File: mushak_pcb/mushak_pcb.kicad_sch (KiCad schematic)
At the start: 45 parts, among them J1 Conn_01x04_Male, J10 IR_1, J11 AS5600_1, J12 IR_2, J13 AS5600_2, J14 IR_3, J15 ToF, J16 IR_4, J2 Conn_01x02_Female, J3 BLE_Conn, Q1 DMN3065LW-7, SW1 SW_Push, SW2 SW_Push, U2 TLV1117LV30DCYT, U6 STM32F405RGTx, Y1 25Mhz, Y2 32.769kHz

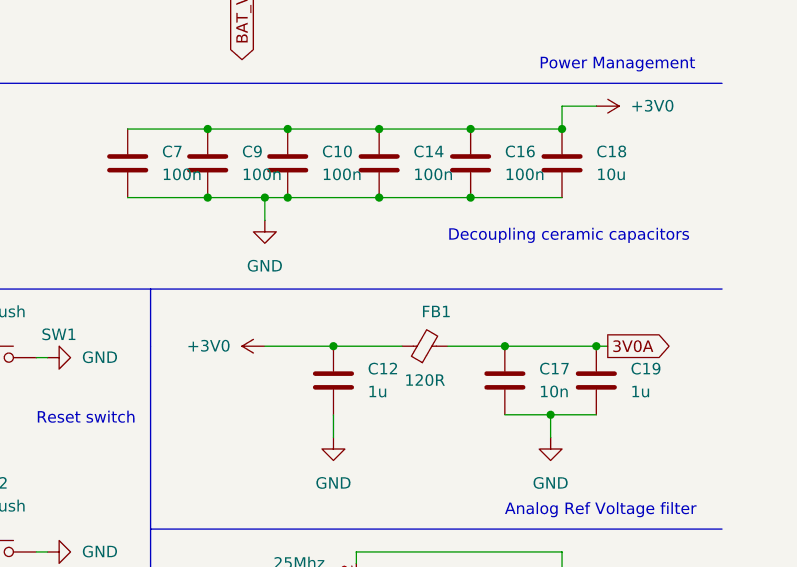
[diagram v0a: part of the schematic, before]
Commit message: changed footprints of capacitors and resistors
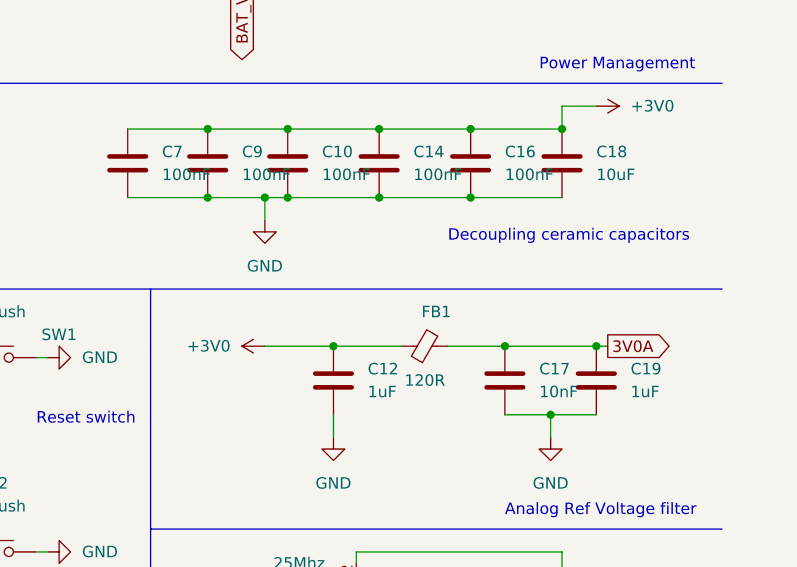
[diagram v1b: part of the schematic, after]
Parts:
- C10, C16, C7, C9: value 100n -> 100nF; footprint Capacitor_SMD:C_0402_1005Metric -> Capacitor_SMD:C_0201_0603Metric
- C12, C19: value 1u -> 1uF
- C13, C8: footprint Capacitor_SMD:C_0402_1005Metric -> Capacitor_SMD:C_0805_2012Metric
- C14: value 100n -> 100nF
- C17: value 10n -> 10nF
- C18: value 10u -> 10uF
- C3, C4: footprint Capacitor_SMD:C_0402_1005Metric -> Capacitor_SMD:C_0201_0603Metric
- R1, R4: footprint Resistor_SMD:R_0402_1005Metric -> Resistor_SMD:R_0603_1608Metric
- R2, R3: footprint Resistor_SMD:R_0402_1005Metric -> Resistor_SMD:R_0201_0603Metric

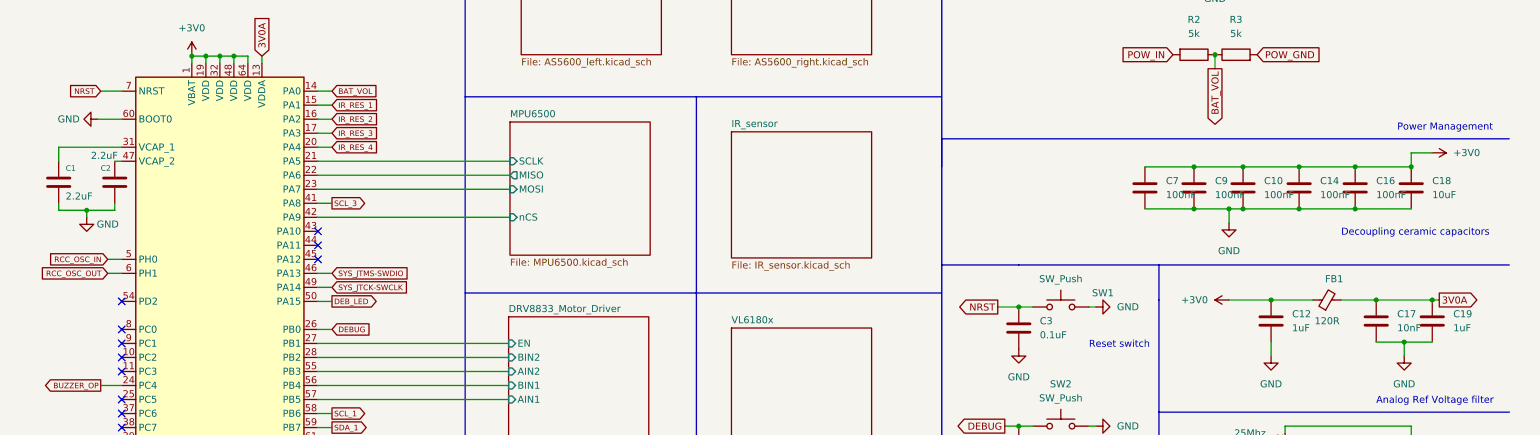
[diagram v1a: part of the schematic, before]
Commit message: made draft pcb footprint placement
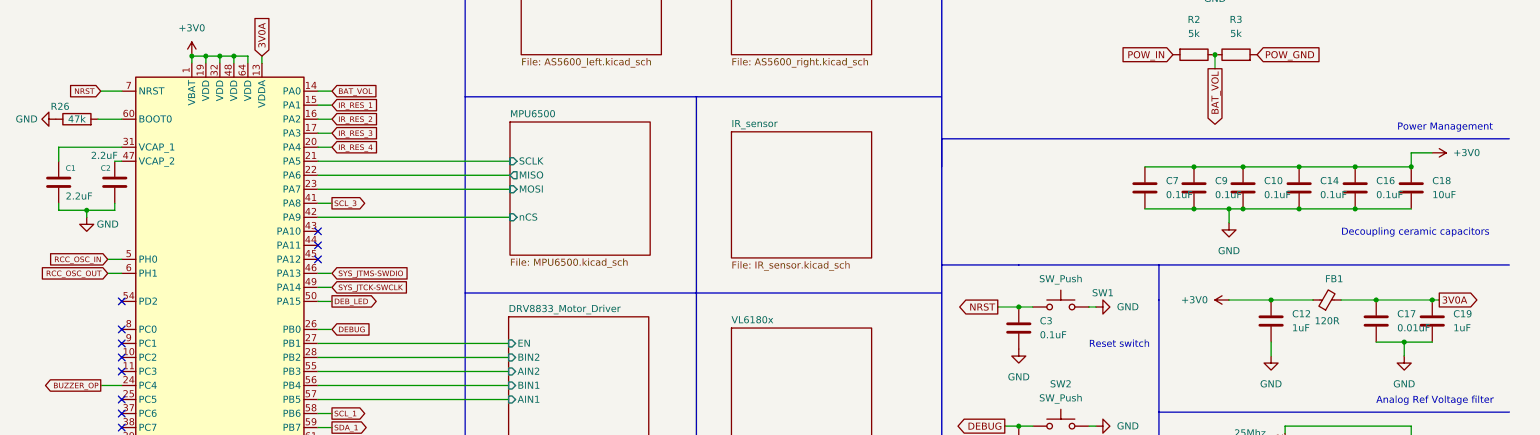
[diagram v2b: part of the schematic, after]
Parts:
- added R26: 47k, Resistor_SMD:R_0201_0603Metric, symbol Device:R
- C10, C14, C16, C7, C9: value 100nF -> 0.1uF
- C17: value 10nF -> 0.01uF
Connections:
- net GND: now also R26.1; no longer U6.60 (BOOT0)
- new net: R26.2, U6.60 (BOOT0)

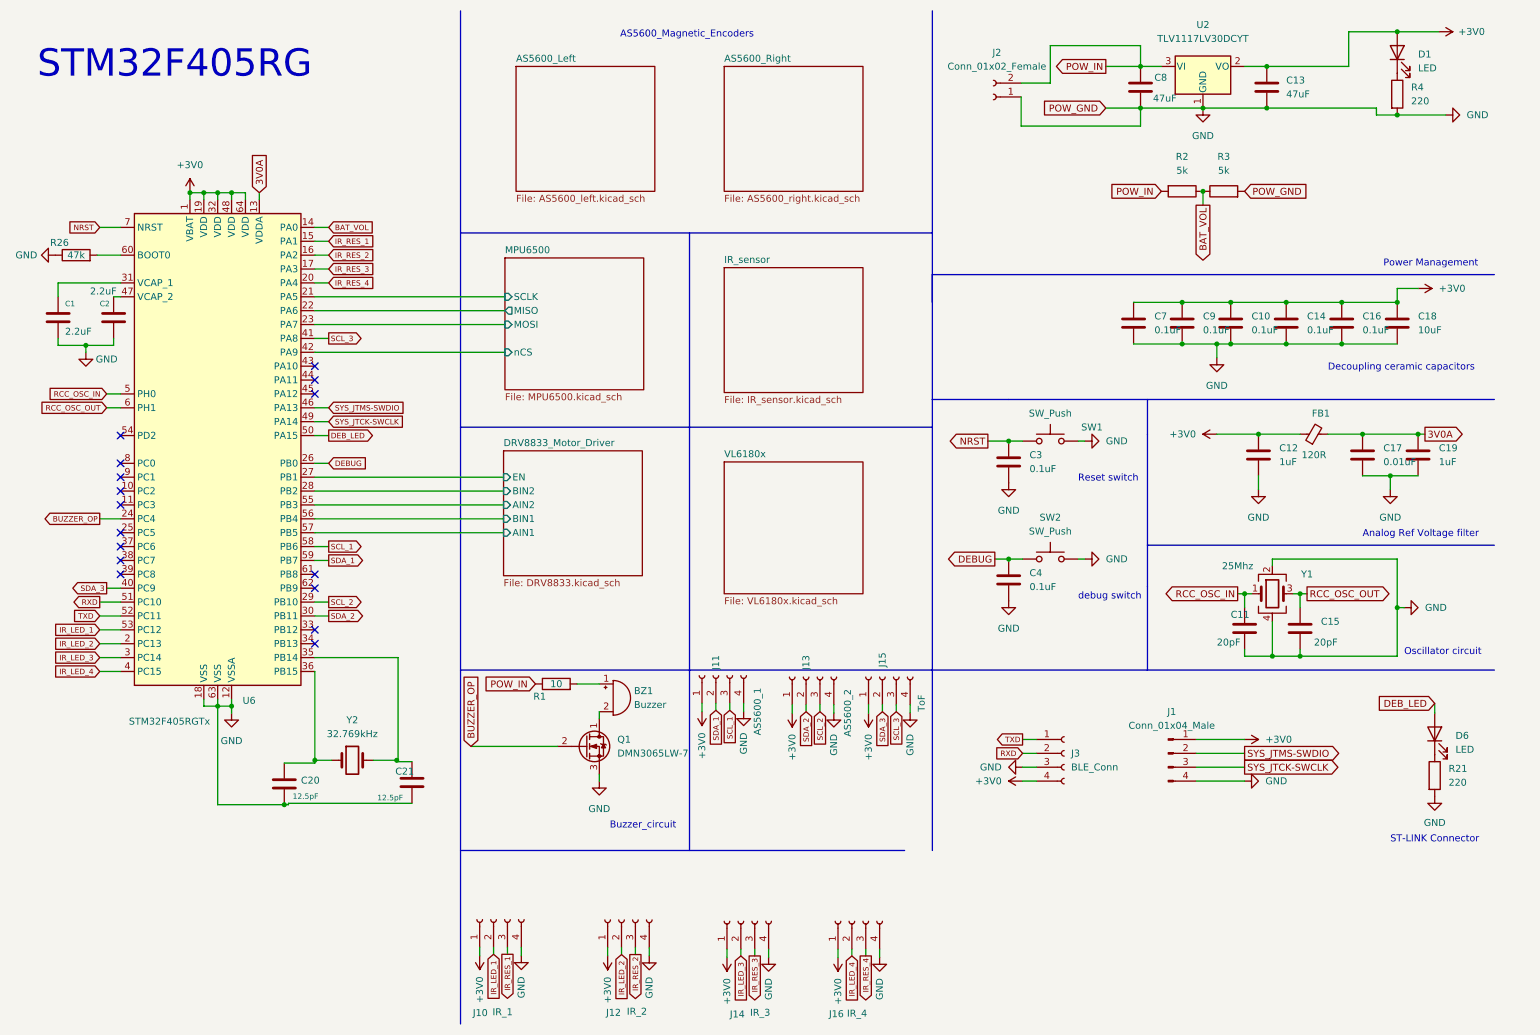
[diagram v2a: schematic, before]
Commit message: Add 3d models to footprint
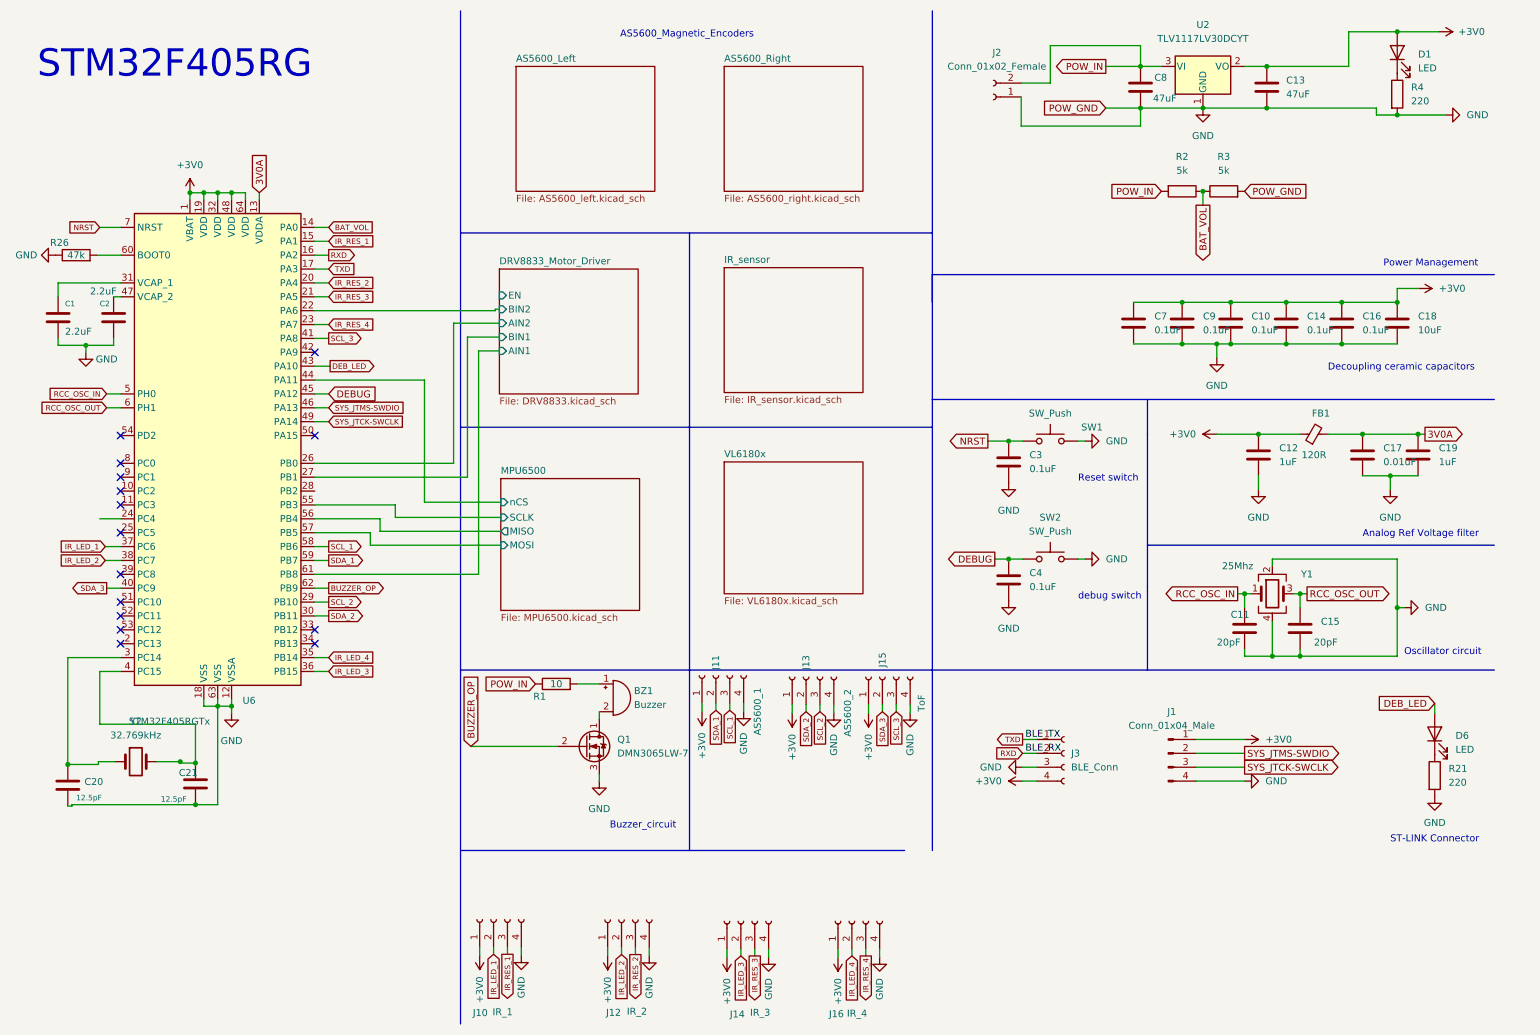
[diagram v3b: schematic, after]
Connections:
- net BUZZER_OP: now also U6.62 (PB9); no longer U6.24 (PC4)
- net DEBUG: now also U6.45 (PA12); no longer U6.26 (PB0)
- net DEB_LED: now also U6.43 (PA10); no longer U6.50 (PA15)
- net DRV8833_Motor_Driver/AIN1: now also U6.61 (PB8); no longer U6.57 (PB5)
- net DRV8833_Motor_Driver/AIN2: now also U6.26 (PB0); no longer U6.55 (PB3)
- net DRV8833_Motor_Driver/BIN1: now also U6.27 (PB1); no longer U6.56 (PB4)
- net DRV8833_Motor_Driver/BIN2: now also U6.22 (PA6); no longer U6.28 (PB2)
- net DRV8833_Motor_Driver/EN: no longer U6.27 (PB1)
- net IR_LED_1: now also U6.37 (PC6); no longer U6.53 (PC12)
- net IR_LED_2: now also U6.38 (PC7); no longer U6.2 (PC13)
- net IR_LED_3: now also U6.36 (PB15); no longer U6.3 (PC14)
- net IR_LED_4: now also U6.35 (PB14); no longer U6.4 (PC15)
- net IR_RES_2: now also U6.20 (PA4); no longer U6.16 (PA2)
- net IR_RES_3: now also U6.21 (PA5); no longer U6.17 (PA3)
- net IR_RES_4: now also U6.23 (PA7); no longer U6.20 (PA4)
- net MPU6500/MISO: now also U6.56 (PB4); no longer U6.22 (PA6)
- net MPU6500/MOSI: now also U6.57 (PB5); no longer U6.23 (PA7)
- net MPU6500/SCLK: now also U6.55 (PB3); no longer U6.21 (PA5)
- net MPU6500/nCS: now also U6.44 (PA11); no longer U6.42 (PA9)
- net RXD: now also U6.16 (PA2); no longer U6.51 (PC10)
- net TXD: now also U6.17 (PA3); no longer U6.52 (PC11)
- net at C20.1, Y2.1: now also U6.3 (PC14); no longer U6.36 (PB15)
- net at C21.1, Y2.2: now also U6.4 (PC15); no longer U6.35 (PB14)
- no-connect marks 16 -> 15
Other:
- moved on the sheet: C20, C21, Y2

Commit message: updated footprint for motors
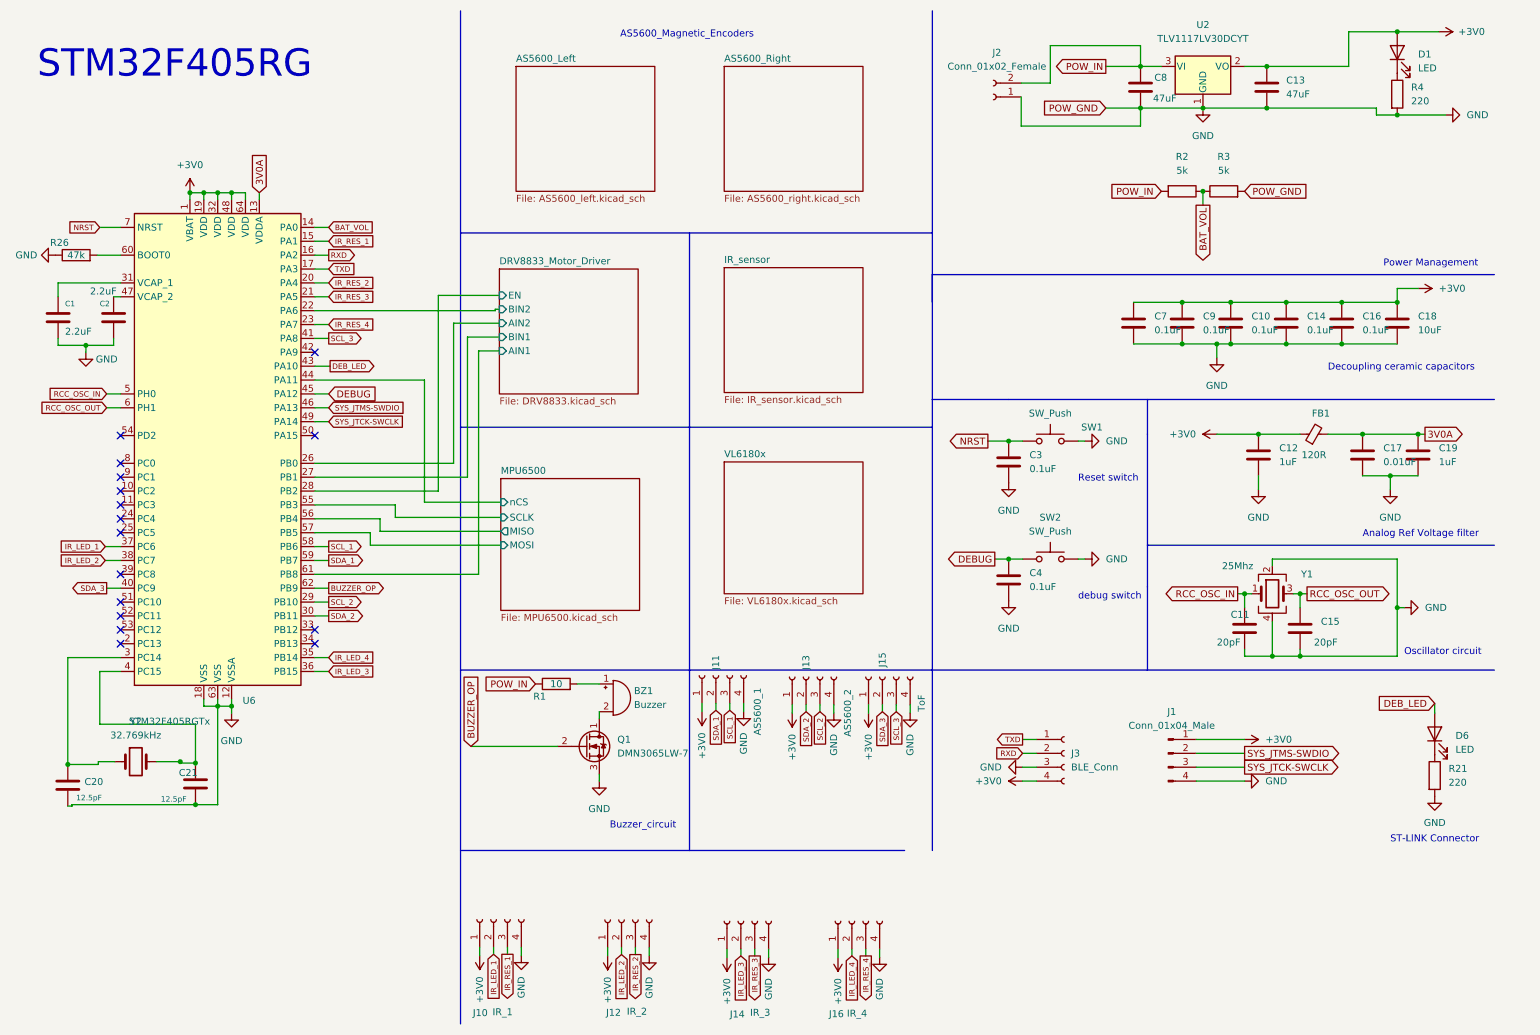
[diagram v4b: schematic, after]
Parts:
- SW1, SW2: footprint Button_Switch_SMD:SW_SPST_CK_RS282G05A3 -> TL1015AF160QG:SW_TL1015AF160QG
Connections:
- net DRV8833_Motor_Driver/EN: now also U6.28 (PB2)
- no-connect marks 15 -> 16
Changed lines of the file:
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@@
   (no_connect (at 33.02 108.204))
   (no_connect (at 33.02 115.824))
+  (no_connect (at 33.02 105.664))
   (no_connect (at 68.58 75.184))
   (wire (pts (xy 68.58 133.604) (xy 71.12 133.604))
@@
     (stroke (width 0) (type default) (color 0 0 0 0))
   )
+  (wire (pts (xy 91.186 64.77) (xy 91.186 100.584))
+    (stroke (width 0) (type default) (color 0 0 0 0))
+  )
+  (wire (pts (xy 102.362 64.77) (xy 91.186 64.77))
+    (stroke (width 0) (type default) (color 0 0 0 0))
+  )
   (wire (pts (xy 68.58 98.044) (xy 96.52 98.044))
     (stroke (width 0) (type default) (color 0 0 0 0))
@@
     (stroke (width 0) (type default) (color 0 0 0 0))
   )
+  (wire (pts (xy 91.186 100.584) (xy 68.58 100.584))
+    (stroke (width 0) (type default) (color 0 0 0 0))
+  )
   (wire (pts (xy 44.196 150.114) (xy 43.942 150.114))
     (stroke (width 0) (type default) (color 0 0 0 0))
@@
   )
   (wire (pts (xy 46.736 150.368) (xy 43.942 150.368))
-    (stroke (width 0) (type default) (color 0 0 0 0))
-  )
-  (wire (pts (xy 29.21 105.664) (xy 33.02 105.664))
     (stroke (width 0) (type default) (color 0 0 0 0))
   )
@@
   )
   (text "Oscillator circuit\n" (at 267.97 130.81 0)
-    (effects (font (size 1.27 1.27)) (justify left bottom))
-  )
-  (label "BLE_TX" (at 198.628 146.05 0)
-    (effects (font (size 1.27 1.27)) (justify left bottom))
-  )
-  (label "BLE_RX" (at 198.628 148.59 0)
     (effects (font (size 1.27 1.27)) (justify left bottom))
   )
@@
     (property "Reference" "SW2" (id 0) (at 203.2 105.41 0))
     (property "Value" "SW_Push" (id 1) (at 203.2 107.95 0))
-    (property "Footprint" "Button_Switch_SMD:SW_SPST_CK_RS282G05A3" (id 2) (at 203.2 107.95 0)
+    (property "Footprint" "TL1015AF160QG:SW_TL1015AF160QG" (id 2) (at 203.2 107.95 0)
       (effects (font (size 1.27 1.27)) hide)
     )
@@
     (property "Reference" "SW1" (id 0) (at 210.82 88.9 0))
     (property "Value" "SW_Push" (id 1) (at 203.2 86.36 0))
-    (property "Footprint" "Button_Switch_SMD:SW_SPST_CK_RS282G05A3" (id 2) (at 203.2 86.36 0)
+    (property "Footprint" "TL1015AF160QG:SW_TL1015AF160QG" (id 2) (at 203.2 86.36 0)
       (effects (font (size 1.27 1.27)) hide)
     )
@@
       (reference "C21") (unit 1) (value "12.5pF") (footprint "Capacitor_SMD:C_0402_1005Metric")
     )
-    (path "/b79b66d4-5cc5-4098-8c09-408f16b669f0/ccde8f39-c03d-439b-b8c0-bd3bb19d3faa"
-      (reference "C22") (unit 1) (value "10uF") (footprint "Capacitor_SMD:C_0402_1005Metric")
-    )
     (path "/b79b66d4-5cc5-4098-8c09-408f16b669f0/5c07921a-d9ee-4218-b14f-44f9225af66e"
       (reference "C23") (unit 1) (value "0.1uF") (footprint "Capacitor_SMD:C_0402_1005Metric")
     )
-    (path "/21ce20a6-b7bb-4e01-a357-9d2d3872aa77/be851069-5f76-45e2-91a8-855ff1142f2c"
-      (reference "C24") (unit 1) (value "10uF") (footprint "Capacitor_SMD:C_0402_1005Metric")
-    )
     (path "/21ce20a6-b7bb-4e01-a357-9d2d3872aa77/9f4b59ca-5736-48e5-8a60-ad6ed7c6312a"
       (reference "C25") (unit 1) (value "0.1uF") (footprint "Capacitor_SMD:C_0201_0603Metric")
@@
       (reference "J17") (unit 1) (value "ToF") (footprint "mushak_mount_footprint:STAND_SLAVE_04")
     )
+    (path "/ed054e13-fb35-4e88-891e-47af6a8dfbd6/b0240ac4-976d-4884-8446-e4029611ccf2"
+      (reference "M1") (unit 1) (value "motor") (footprint "mushak_mount_footprint:motor")
+    )
+    (path "/ed054e13-fb35-4e88-891e-47af6a8dfbd6/c5cbe8da-a568-4878-be33-6b742ab8eee6"
+      (reference "M2") (unit 1) (value "motor") (footprint "mushak_mount_footprint:motor")
+    )
     (path "/f85a8f06-68b6-4dee-b46b-b569fac369a8"
       (reference "Q1") (unit 1) (value "DMN3065LW-7") (footprint "Package_TO_SOT_SMD:SOT-323_SC-70")
@@
     )
     (path "/b266ad3c-1d50-4b2b-8a1e-c69f93195963"
-      (reference "SW1") (unit 1) (value "SW_Push") (footprint "Button_Switch_SMD:SW_SPST_CK_RS282G05A3")
+      (reference "SW1") (unit 1) (value "SW_Push") (footprint "TL1015AF160QG:SW_TL1015AF160QG")
     )
     (path "/1273f667-bd83-4eaf-a97c-819701fc1fd5"
-      (reference "SW2") (unit 1) (value "SW_Push") (footprint "Button_Switch_SMD:SW_SPST_CK_RS282G05A3")
-    )
-    (path "/ed054e13-fb35-4e88-891e-47af6a8dfbd6/b316c1b7-53ed-4315-abba-5e66fedb1d35"
-      (reference "TP23") (unit 1) (value "MOT_1") (footprint "TestPoint:TestPoint_Pad_1.0x1.0mm")
-    )
-    (path "/ed054e13-fb35-4e88-891e-47af6a8dfbd6/8ed12b6e-5fbe-4bb4-88a7-54a2a43bd1c0"
-      (reference "TP24") (unit 1) (value "MOT_1") (footprint "TestPoint:TestPoint_Pad_1.0x1.0mm")
-    )
-    (path "/ed054e13-fb35-4e88-891e-47af6a8dfbd6/d708ada7-201f-4599-b32d-30c531b46253"
-      (reference "TP25") (unit 1) (value "MOT_2") (footprint "TestPoint:TestPoint_Pad_1.0x1.0mm")
-    )
-    (path "/ed054e13-fb35-4e88-891e-47af6a8dfbd6/434155f3-2fc9-429a-8336-7001412173f0"
-      (reference "TP26") (unit 1) (value "MOT_2") (footprint "TestPoint:TestPoint_Pad_1.0x1.0mm")
+      (reference "SW2") (unit 1) (value "SW_Push") (footprint "TL1015AF160QG:SW_TL1015AF160QG")
     )
     (path "/af2b6e1b-fbd3-4882-ace2-a14e9a039991"
